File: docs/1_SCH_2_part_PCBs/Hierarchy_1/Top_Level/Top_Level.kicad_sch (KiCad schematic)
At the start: 0 parts

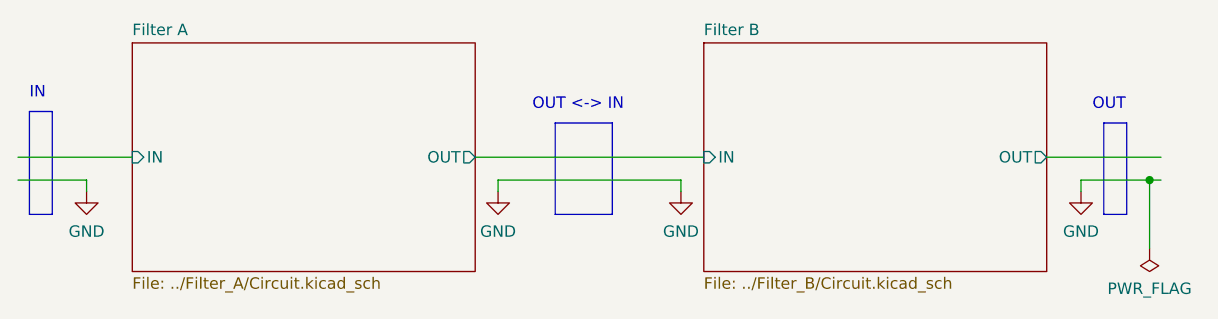
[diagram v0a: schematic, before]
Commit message: [DOCs] Changed the hierarchical strategy
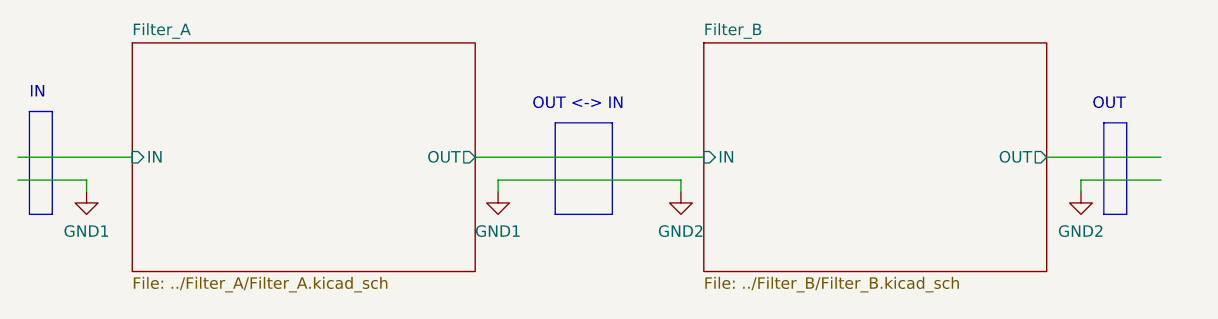
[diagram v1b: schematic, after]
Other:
- sheet Filter A renamed Filter_A
- sheet Filter B renamed Filter_B
- sheet Filter_A: file ../Filter_A/Circuit.kicad_sch -> ../Filter_A/Filter_A.kicad_sch
- sheet Filter_B: file ../Filter_B/Circuit.kicad_sch -> ../Filter_B/Filter_B.kicad_sch
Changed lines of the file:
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@@
     (title "Filter A + B (Top level)")
   )
-  (junction (at 189.23 78.74) (diameter 0) (color 0 0 0 0)
-  )
-  (wire (pts (xy 181.61 78.74) (xy 189.23 78.74))
+  (wire (pts (xy 181.61 78.74) (xy 190.5 78.74))
     (stroke (width 0) (type default) (color 0 0 0 0))
   )
@@
     (stroke (width 0) (type default) (color 0 0 0 0))
   )
-  (wire (pts (xy 189.23 78.74) (xy 190.5 78.74))
-    (stroke (width 0) (type default) (color 0 0 0 0))
-  )
   (polyline (pts (xy 64.77 71.12) (xy 67.31 71.12))
     (stroke (width 0) (type default) (color 0 0 0 0))
@@
   )
   (wire (pts (xy 137.16 78.74) (xy 137.16 80.01))
-    (stroke (width 0) (type default) (color 0 0 0 0))
-  )
-  (wire (pts (xy 189.23 78.74) (xy 189.23 86.36))
     (stroke (width 0) (type default) (color 0 0 0 0))
   )
@@
     (effects (font (size 1.27 1.27)) (justify left bottom))
   )
-  (symbol (lib_id "power:GND") (at 137.16 80.01 0) (unit 1)
-    (in_bom yes) (on_board yes) (fields_autoplaced)
-    (property "Reference" "#PWR0102" (id 0) (at 137.16 86.36 0)
-      (effects (font (size 1.27 1.27)) hide)
-    )
-    (property "Value" "GND" (id 1) (at 137.16 84.4534 0))
+  (symbol (lib_id "power:GND1") (at 71.12 80.01 0) (unit 1)
+    (in_bom yes) (on_board yes) (fields_autoplaced)
+    (property "Reference" "#PWR0106" (id 0) (at 71.12 86.36 0)
+      (effects (font (size 1.27 1.27)) hide)
+    )
+    (property "Value" "GND1" (id 1) (at 71.12 84.4534 0))
+    (property "Footprint" "" (id 2) (at 71.12 80.01 0)
+      (effects (font (size 1.27 1.27)) hide)
+    )
+    (property "Datasheet" "" (id 3) (at 71.12 80.01 0)
+      (effects (font (size 1.27 1.27)) hide)
+    )
+    (pin "1")
+  )
+  (symbol (lib_id "power:GND2") (at 137.16 80.01 0) (unit 1)
+    (in_bom yes) (on_board yes) (fields_autoplaced)
+    (property "Reference" "#PWR0108" (id 0) (at 137.16 86.36 0)
+      (effects (font (size 1.27 1.27)) hide)
+    )
+    (property "Value" "GND2" (id 1) (at 137.16 84.4534 0))
     (property "Footprint" "" (id 2) (at 137.16 80.01 0)
       (effects (font (size 1.27 1.27)) hide)
@@
     (pin "1")
   )
-  (symbol (lib_id "power:PWR_FLAG") (at 189.23 86.36 180) (unit 1)
-    (in_bom yes) (on_board yes) (fields_autoplaced)
-    (property "Reference" "#FLG0101" (id 0) (at 189.23 88.265 0)
-      (effects (font (size 1.27 1.27)) hide)
-    )
-    (property "Value" "PWR_FLAG" (id 1) (at 189.23 90.8034 0))
-    (property "Footprint" "" (id 2) (at 189.23 86.36 0)
-      (effects (font (size 1.27 1.27)) hide)
-    )
-    (property "Datasheet" "~" (id 3) (at 189.23 86.36 0)
-      (effects (font (size 1.27 1.27)) hide)
-    )
-    (pin "1")
-  )
-  (symbol (lib_id "power:GND") (at 181.61 80.01 0) (unit 1)
-    (in_bom yes) (on_board yes) (fields_autoplaced)
-    (property "Reference" "#PWR0111" (id 0) (at 181.61 86.36 0)
-      (effects (font (size 1.27 1.27)) hide)
-    )
-    (property "Value" "GND" (id 1) (at 181.61 84.4534 0))
+  (symbol (lib_id "power:GND2") (at 181.61 80.01 0) (unit 1)
+    (in_bom yes) (on_board yes) (fields_autoplaced)
+    (property "Reference" "#PWR0107" (id 0) (at 181.61 86.36 0)
+      (effects (font (size 1.27 1.27)) hide)
+    )
+    (property "Value" "GND2" (id 1) (at 181.61 84.4534 0))
     (property "Footprint" "" (id 2) (at 181.61 80.01 0)
       (effects (font (size 1.27 1.27)) hide)
@@
     (pin "1")
   )
-  (symbol (lib_id "power:GND") (at 71.12 80.01 0) (unit 1)
-    (in_bom yes) (on_board yes) (fields_autoplaced)
-    (property "Reference" "#PWR0103" (id 0) (at 71.12 86.36 0)
-      (effects (font (size 1.27 1.27)) hide)
-    )
-    (property "Value" "GND" (id 1) (at 71.12 84.4534 0))
-    (property "Footprint" "" (id 2) (at 71.12 80.01 0)
-      (effects (font (size 1.27 1.27)) hide)
-    )
-    (property "Datasheet" "" (id 3) (at 71.12 80.01 0)
-      (effects (font (size 1.27 1.27)) hide)
-    )
-    (pin "1")
-  )
-  (symbol (lib_id "power:GND") (at 116.84 80.01 0) (unit 1)
-    (in_bom yes) (on_board yes) (fields_autoplaced)
-    (property "Reference" "#PWR0101" (id 0) (at 116.84 86.36 0)
-      (effects (font (size 1.27 1.27)) hide)
-    )
-    (property "Value" "GND" (id 1) (at 116.84 84.4534 0))
+  (symbol (lib_id "power:GND1") (at 116.84 80.01 0) (unit 1)
+    (in_bom yes) (on_board yes) (fields_autoplaced)
+    (property "Reference" "#PWR0105" (id 0) (at 116.84 86.36 0)
+      (effects (font (size 1.27 1.27)) hide)
+    )
+    (property "Value" "GND1" (id 1) (at 116.84 84.4534 0))
     (property "Footprint" "" (id 2) (at 116.84 80.01 0)
       (effects (font (size 1.27 1.27)) hide)
@@
     (stroke (width 0.1524) (type solid) (color 0 0 0 0))
     (fill (color 0 0 0 0.0000))
-    (property "Sheet name" "Filter A" (id 0) (at 76.2 62.7884 0)
+    (property "Sheet name" "Filter_A" (id 0) (at 76.2 62.7884 0)
       (effects (font (size 1.27 1.27)) (justify left bottom))
     )
-    (property "Sheet file" "../Filter_A/Circuit.kicad_sch" (id 1) (at 76.2 89.4846 0)
+    (property "Sheet file" "../Filter_A/Filter_A.kicad_sch" (id 1) (at 76.2 89.4846 0)
       (effects (font (size 1.27 1.27)) (justify left top))
     )
@@
     (stroke (width 0.1524) (type solid) (color 0 0 0 0))
     (fill (color 0 0 0 0.0000))
-    (property "Sheet name" "Filter B" (id 0) (at 139.7 62.7884 0)
+    (property "Sheet name" "Filter_B" (id 0) (at 139.7 62.7884 0)
       (effects (font (size 1.27 1.27)) (justify left bottom))
     )
-    (property "Sheet file" "../Filter_B/Circuit.kicad_sch" (id 1) (at 139.7 89.4846 0)
+    (property "Sheet file" "../Filter_B/Filter_B.kicad_sch" (id 1) (at 139.7 89.4846 0)
       (effects (font (size 1.27 1.27)) (justify left top))
     )
@@
   )
   (symbol_instances
-    (path "/1165f0b9-cae3-40fb-be7a-c5bf163cbf9f"
+    (path "/1915c359-c3f3-4d3d-9201-50272cf57a7c/665930ba-f909-46e6-ac09-95855d6c4144"
       (reference "#FLG0101") (unit 1) (value "PWR_FLAG") (footprint "")
     )
-    (path "/d5e61638-18ca-4834-9283-458b681cd702"
-      (reference "#PWR0101") (unit 1) (value "GND") (footprint "")
-    )
-    (path "/0c53934a-fe12-4364-81ad-65605dc2c4ac"
-      (reference "#PWR0102") (unit 1) (value "GND") (footprint "")
-    )
-    (path "/af1c7d98-5b8c-46fa-a813-df70e01c8a68"
-      (reference "#PWR0103") (unit 1) (value "GND") (footprint "")
-    )
-    (path "/1915c359-c3f3-4d3d-9201-50272cf57a7c/b26a0bef-5a77-44df-b8ec-fac784d41abf"
-      (reference "#PWR0104") (unit 1) (value "GND") (footprint "")
-    )
-    (path "/1915c359-c3f3-4d3d-9201-50272cf57a7c/2f928cd3-27f2-4b7a-ac94-7d1dc864d6b5"
-      (reference "#PWR0105") (unit 1) (value "GND") (footprint "")
-    )
-    (path "/1915c359-c3f3-4d3d-9201-50272cf57a7c/8fa76464-2917-48a3-abf8-3a6cee89a18f"
-      (reference "#PWR0106") (unit 1) (value "GND") (footprint "")
-    )
-    (path "/1915c359-c3f3-4d3d-9201-50272cf57a7c/0fa0a6f4-9907-454f-bd65-f35d5ea698a8"
-      (reference "#PWR0107") (unit 1) (value "GND") (footprint "")
-    )
-    (path "/eb9bfe27-f26e-461b-be25-bc92a359b8c5/45bd41c1-4f4f-468d-8c9a-f5428ba2bb91"
-      (reference "#PWR0108") (unit 1) (value "GND") (footprint "")
-    )
-    (path "/eb9bfe27-f26e-461b-be25-bc92a359b8c5/7f137ceb-57ec-4216-8bc6-9a75b1f036fe"
-      (reference "#PWR0109") (unit 1) (value "GND") (footprint "")
-    )
-    (path "/eb9bfe27-f26e-461b-be25-bc92a359b8c5/f1982af2-4a59-4e43-837b-f59f16d55096"
-      (reference "#PWR0110") (unit 1) (value "GND") (footprint "")
-    )
-    (path "/254f3422-0597-406b-b24e-167453759168"
-      (reference "#PWR0111") (unit 1) (value "GND") (footprint "")
+    (path "/eb9bfe27-f26e-461b-be25-bc92a359b8c5/6c27ecfe-afc0-449e-9f52-b4d0eaff37b1"
+      (reference "#FLG0102") (unit 1) (value "PWR_FLAG") (footprint "")
+    )
+    (path "/1915c359-c3f3-4d3d-9201-50272cf57a7c/a511d9b6-2293-48e7-9a5a-dadefb785dc4"
+      (reference "#PWR01") (unit 1) (value "GND1") (footprint "")
+    )
+    (path "/1915c359-c3f3-4d3d-9201-50272cf57a7c/9aed012e-76db-456c-9606-8ce7a7c48370"
+      (reference "#PWR02") (unit 1) (value "GND1") (footprint "")
+    )
+    (path "/1915c359-c3f3-4d3d-9201-50272cf57a7c/b4c9f615-8394-4d40-885e-6ce3cf46fe2e"
+      (reference "#PWR03") (unit 1) (value "GND1") (footprint "")
+    )
+    (path "/1915c359-c3f3-4d3d-9201-50272cf57a7c/cf559a94-0b0f-4a5f-ad42-e70e02125571"
+      (reference "#PWR04") (unit 1) (value "GND1") (footprint "")
+    )
+    (path "/1915c359-c3f3-4d3d-9201-50272cf57a7c/dbc8c808-18ae-46fc-944b-83161d4cf420"
+      (reference "#PWR05") (unit 1) (value "GND1") (footprint "")
+    )
+    (path "/eb9bfe27-f26e-461b-be25-bc92a359b8c5/ae0f78d5-7a28-4d3f-89e6-85902dc1169d"
+      (reference "#PWR0101") (unit 1) (value "GND2") (footprint "")
+    )
+    (path "/eb9bfe27-f26e-461b-be25-bc92a359b8c5/7de809d3-593f-4c4b-9be4-82ff94ac9eeb"
+      (reference "#PWR0102") (unit 1) (value "GND2") (footprint "")
+    )
+    (path "/eb9bfe27-f26e-461b-be25-bc92a359b8c5/05abc4af-56f4-4c0a-86dc-434196135fab"
+      (reference "#PWR0103") (unit 1) (value "GND2") (footprint "")
+    )
+    (path "/eb9bfe27-f26e-461b-be25-bc92a359b8c5/8f827479-706f-433b-84b1-398bbb1582bb"
+      (reference "#PWR0104") (unit 1) (value "GND2") (footprint "")
+    )
+    (path "/e6b5b8cc-d36b-458c-95e9-473fcf53c186"
+      (reference "#PWR0105") (unit 1) (value "GND1") (footprint "")
+    )
+    (path "/08ee5ad7-a452-4553-84ed-02c04b11d9f4"
+      (reference "#PWR0106") (unit 1) (value "GND1") (footprint "")
+    )
+    (path "/41a0830e-84f6-4a1e-a8cb-d7d2ba3b115e"
+      (reference "#PWR0107") (unit 1) (value "GND2") (footprint "")
+    )
+    (path "/1eed23be-ed7e-4b7b-9bf8-10e4a95c4d4f"
+      (reference "#PWR0108") (unit 1) (value "GND2") (footprint "")
     )
     (path "/1915c359-c3f3-4d3d-9201-50272cf57a7c/fe6ba767-ccdc-43b3-8046-b03474a8e7c1"
